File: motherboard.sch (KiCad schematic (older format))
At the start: 105 parts, among them P1 CONN_02X08, U1 STM32F411-LQFP64, U10 74LS125, U11 74LS125, U12 74LS125, U13 74LS125, U14 PCA9517A, U15 PCA9517A, U16 74LS125, U17 74LS125, U2 STM32F411-LQFP64, U3 AP7313, U4 74LS00, U5 74LS125, U6 FM25V20A-G, U7 FM25V20A-G, U8 FM25V20A-G, U9 FM25V20A-G, Y1 32k, Y2 8M(16pF), Y3 32k, Y4 8M(16pF)

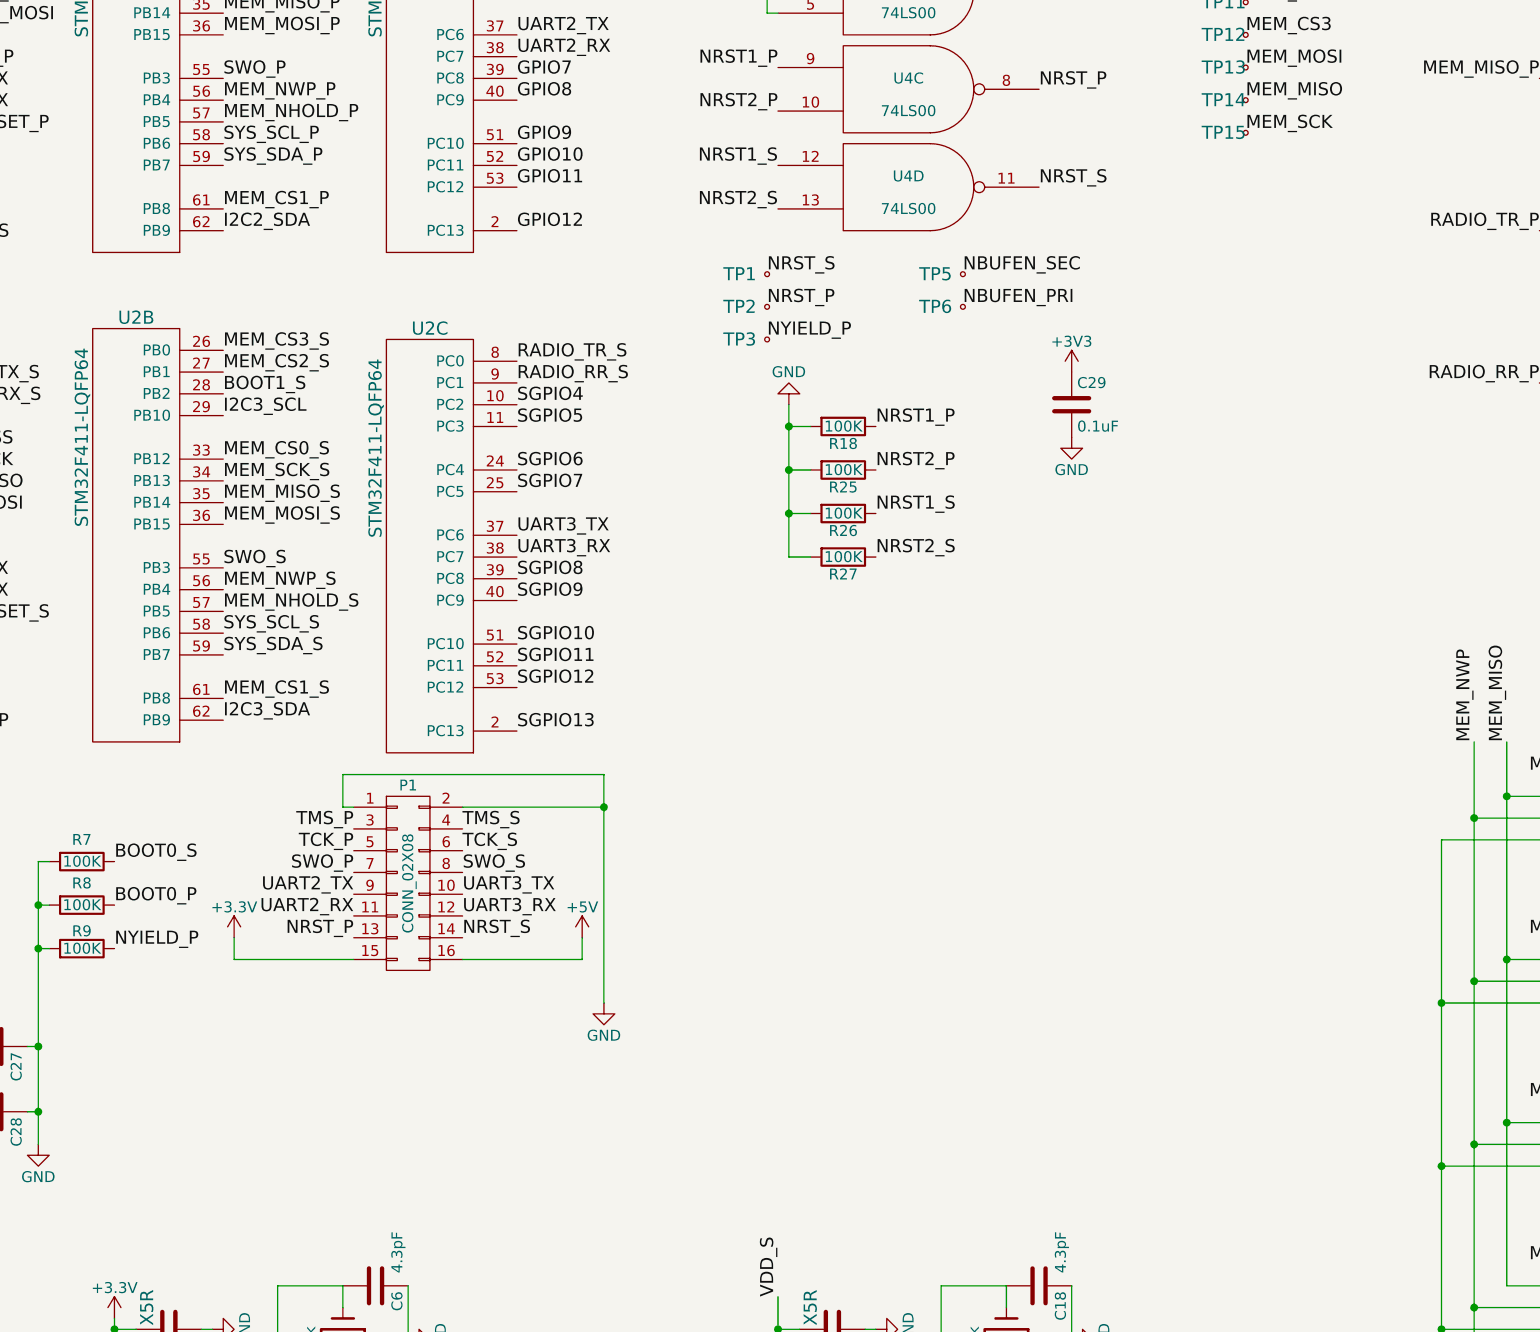
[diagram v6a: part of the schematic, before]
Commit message: Adding ground plane
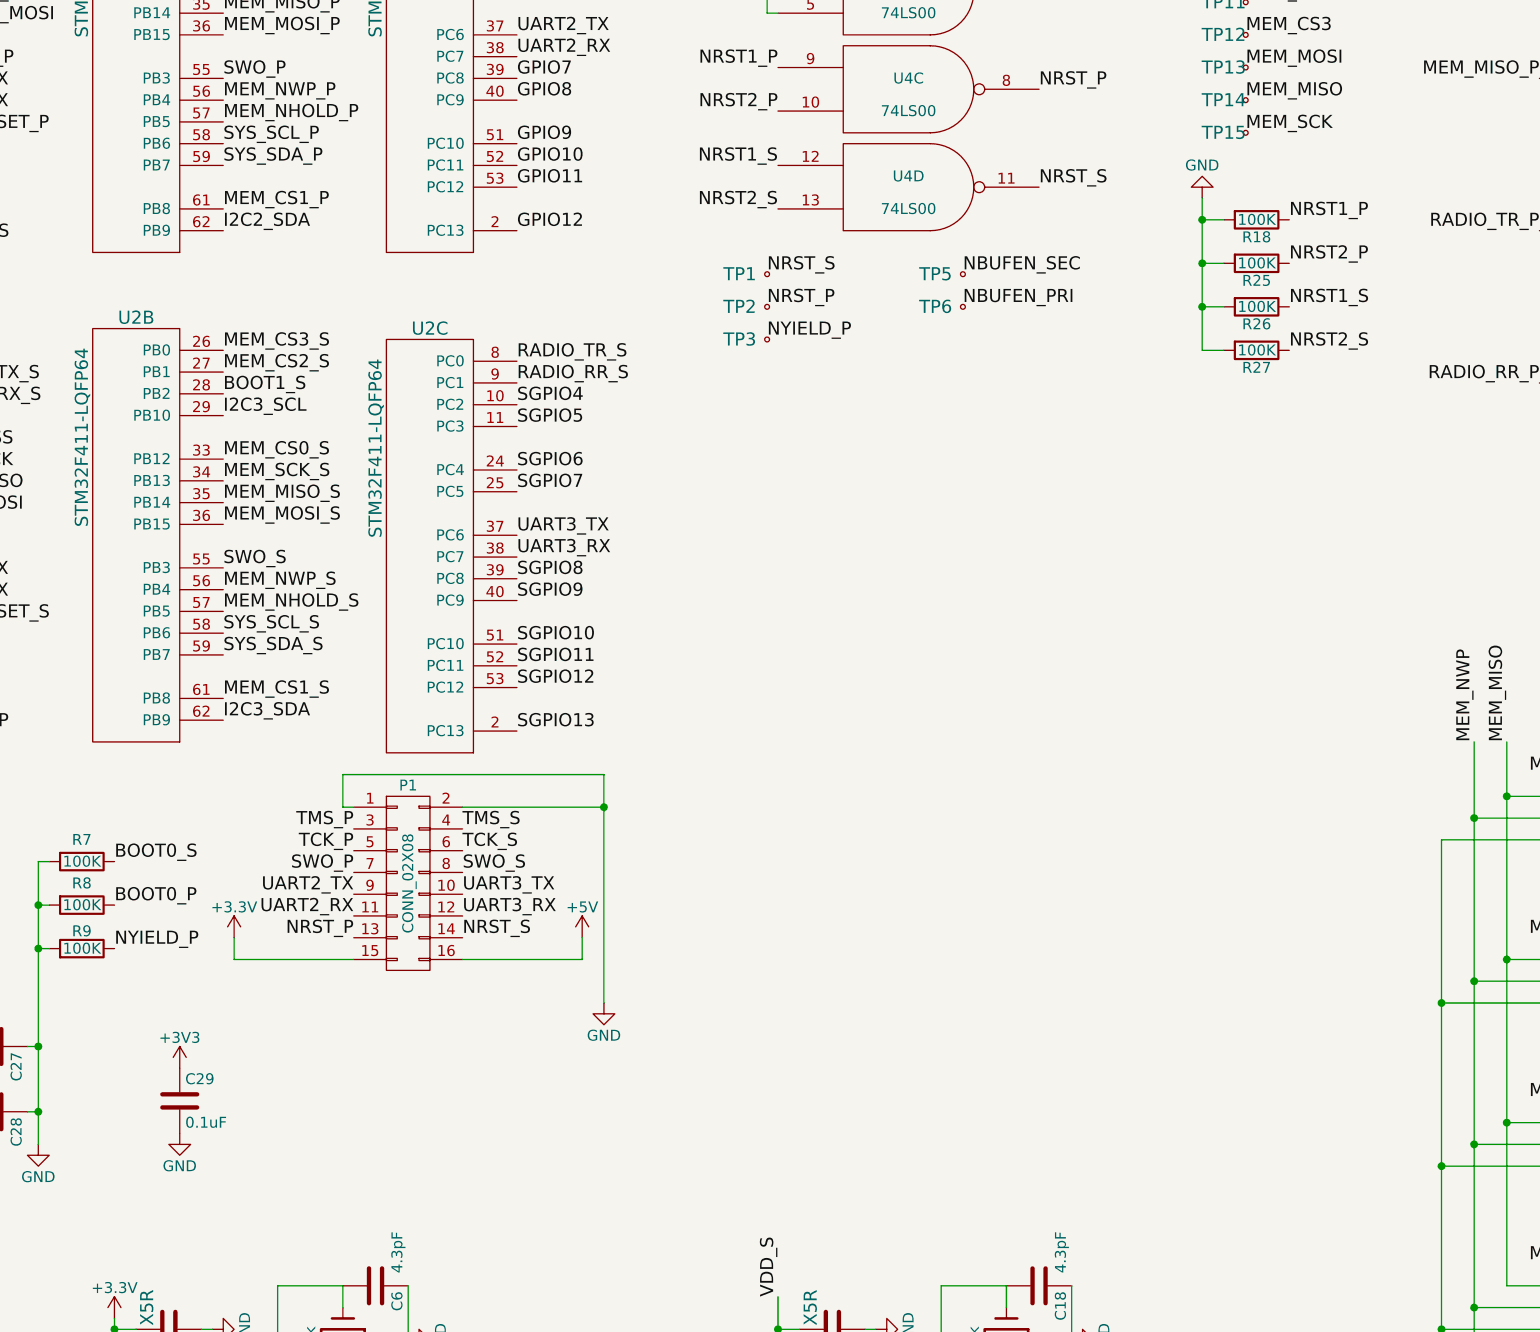
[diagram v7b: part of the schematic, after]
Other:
- moved on the sheet: C29, R18, R25, R26, R27
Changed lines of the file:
@@
 L R R18
 U 1 1 58FDD0DA
-P 5650 3400
-F 0 "R18" V 5730 3400 50  0000 C CNN
-F 1 "100K" V 5650 3400 50  0000 C CNN
-F 2 "Resistors_SMD:R_0805_HandSoldering" V 5580 3400 50  0001 C CNN
-F 3 "" H 5650 3400 50  0000 C CNN
-	1    5650 3400
+P 7550 2450
+F 0 "R18" V 7630 2450 50  0000 C CNN
+F 1 "100K" V 7550 2450 50  0000 C CNN
+F 2 "Resistors_SMD:R_0805_HandSoldering" V 7480 2450 50  0001 C CNN
+F 3 "" H 7550 2450 50  0000 C CNN
+	1    7550 2450
 	0    1    1    0
 $EndComp
@@
 L R R25
 U 1 1 58FF6AE5
-P 5650 3600
-F 0 "R25" V 5730 3600 50  0000 C CNN
-F 1 "100K" V 5650 3600 50  0000 C CNN
-F 2 "Resistors_SMD:R_0805_HandSoldering" V 5580 3600 50  0001 C CNN
-F 3 "" H 5650 3600 50  0000 C CNN
-	1    5650 3600
+P 7550 2650
+F 0 "R25" V 7630 2650 50  0000 C CNN
+F 1 "100K" V 7550 2650 50  0000 C CNN
+F 2 "Resistors_SMD:R_0805_HandSoldering" V 7480 2650 50  0001 C CNN
+F 3 "" H 7550 2650 50  0000 C CNN
+	1    7550 2650
 	0    1    1    0
 $EndComp
@@
 L R R26
 U 1 1 58FF6C71
-P 5650 3800
-F 0 "R26" V 5730 3800 50  0000 C CNN
-F 1 "100K" V 5650 3800 50  0000 C CNN
-F 2 "Resistors_SMD:R_0805_HandSoldering" V 5580 3800 50  0001 C CNN
-F 3 "" H 5650 3800 50  0000 C CNN
-	1    5650 3800
+P 7550 2850
+F 0 "R26" V 7630 2850 50  0000 C CNN
+F 1 "100K" V 7550 2850 50  0000 C CNN
+F 2 "Resistors_SMD:R_0805_HandSoldering" V 7480 2850 50  0001 C CNN
+F 3 "" H 7550 2850 50  0000 C CNN
+	1    7550 2850
 	0    1    1    0
 $EndComp
@@
 L R R27
 U 1 1 58FF6DFC
-P 5650 4000
-F 0 "R27" V 5730 4000 50  0000 C CNN
-F 1 "100K" V 5650 4000 50  0000 C CNN
-F 2 "Resistors_SMD:R_0805_HandSoldering" V 5580 4000 50  0001 C CNN
-F 3 "" H 5650 4000 50  0000 C CNN
-	1    5650 4000
-	0    1    1    0
-$EndComp
-Wire Wire Line
-	5500 3400 5400 3400
-Wire Wire Line
-	5400 4000 5500 4000
-Wire Wire Line
-	5500 3800 5400 3800
-Connection ~ 5400 3800
-Wire Wire Line
-	5500 3600 5400 3600
-Connection ~ 5400 3600
-Text Label 5800 3400 0    60   ~ 0
+P 7550 3050
+F 0 "R27" V 7630 3050 50  0000 C CNN
+F 1 "100K" V 7550 3050 50  0000 C CNN
+F 2 "Resistors_SMD:R_0805_HandSoldering" V 7480 3050 50  0001 C CNN
+F 3 "" H 7550 3050 50  0000 C CNN
+	1    7550 3050
+	0    1    1    0
+$EndComp
+Wire Wire Line
+	7400 2450 7300 2450
+Wire Wire Line
+	7300 3050 7400 3050
+Wire Wire Line
+	7400 2850 7300 2850
+Connection ~ 7300 2850
+Wire Wire Line
+	7400 2650 7300 2650
+Connection ~ 7300 2650
+Text Label 7700 2450 0    60   ~ 0
 NRST1_P
-Text Label 5800 3600 0    60   ~ 0
+Text Label 7700 2650 0    60   ~ 0
 NRST2_P
-Text Label 5800 3800 0    60   ~ 0
+Text Label 7700 2850 0    60   ~ 0
 NRST1_S
-Text Label 5800 4000 0    60   ~ 0
+Text Label 7700 3050 0    60   ~ 0
 NRST2_S
 Wire Wire Line
-	5400 3300 5400 4000
-Connection ~ 5400 3400
+	7300 2350 7300 3050
+Connection ~ 7300 2450
 Wire Wire Line
 	14950 7000 15400 7000
@@
 L C C29
 U 1 1 5904FA74
-P 6700 3300
-F 0 "C29" H 6725 3400 50  0000 L CNN
-F 1 "0.1uF" H 6725 3200 50  0000 L CNN
-F 2 "Capacitors_SMD:C_0805_HandSoldering" H 6738 3150 50  0001 C CNN
-F 3 "" H 6700 3300 50  0000 C CNN
-	1    6700 3300
-	1    0    0    -1
-$EndComp
-$Comp
-L +3V3 #PWR057
+P 2600 6500
+F 0 "C29" H 2625 6600 50  0000 L CNN
+F 1 "0.1uF" H 2625 6400 50  0000 L CNN
+F 2 "Capacitors_SMD:C_0805_HandSoldering" H 2638 6350 50  0001 C CNN
+F 3 "" H 2600 6500 50  0000 C CNN
+	1    2600 6500
+	1    0    0    -1
+$EndComp
+$Comp
+L +3V3 #PWR056
 U 1 1 59050061
-P 6700 3150
-F 0 "#PWR057" H 6700 3000 50  0001 C CNN
-F 1 "+3V3" H 6700 3290 50  0000 C CNN
-F 2 "" H 6700 3150 50  0000 C CNN
-F 3 "" H 6700 3150 50  0000 C CNN
-	1    6700 3150
+P 2600 6350
+F 0 "#PWR056" H 2600 6200 50  0001 C CNN
+F 1 "+3V3" H 2600 6490 50  0000 C CNN
+F 2 "" H 2600 6350 50  0000 C CNN
+F 3 "" H 2600 6350 50  0000 C CNN
+	1    2600 6350
+	1    0    0    -1
+$EndComp
+$Comp
+L GND #PWR057
+U 1 1 5905037E
+P 2600 6650
+F 0 "#PWR057" H 2600 6400 50  0001 C CNN
+F 1 "GND" H 2600 6500 50  0000 C CNN
+F 2 "" H 2600 6650 50  0000 C CNN
+F 3 "" H 2600 6650 50  0000 C CNN
+	1    2600 6650
 	1    0    0    -1
 $EndComp
 $Comp
 L GND #PWR058
-U 1 1 5905037E
-P 6700 3450
-F 0 "#PWR058" H 6700 3200 50  0001 C CNN
-F 1 "GND" H 6700 3300 50  0000 C CNN
-F 2 "" H 6700 3450 50  0000 C CNN
-F 3 "" H 6700 3450 50  0000 C CNN
-	1    6700 3450
-	1    0    0    -1
-$EndComp
-$Comp
-L GND #PWR059
 U 1 1 5905285C
 P 15800 1850
-F 0 "#PWR059" H 15800 1600 50  0001 C CNN
+F 0 "#PWR058" H 15800 1600 50  0001 C CNN
 F 1 "GND" H 15800 1700 50  0000 C CNN
 F 2 "" H 15800 1850 50  0000 C CNN
@@
 Connection ~ 15400 1300
 $Comp
-L GND #PWR060
+L GND #PWR059
 U 1 1 590581E4
 P 11750 1850
-F 0 "#PWR060" H 11750 1600 50  0001 C CNN
+F 0 "#PWR059" H 11750 1600 50  0001 C CNN
 F 1 "GND" H 11750 1700 50  0000 C CNN
 F 2 "" H 11750 1850 50  0000 C CNN
@@
 Connection ~ 12050 1300
 $Comp
-L GND #PWR061
+L GND #PWR060
 U 1 1 5905B968
 P 15050 9550
-F 0 "#PWR061" H 15050 9300 50  0001 C CNN
+F 0 "#PWR060" H 15050 9300 50  0001 C CNN
 F 1 "GND" H 15050 9400 50  0000 C CNN
 F 2 "" H 15050 9550 50  0000 C CNN
@@
 Not Populated - Tie Down if Unused
 $Comp
-L GND #PWR062
+L GND #PWR061
 U 1 1 5900142E
 P 11750 2950
-F 0 "#PWR062" H 11750 2700 50  0001 C CNN
+F 0 "#PWR061" H 11750 2700 50  0001 C CNN
 F 1 "GND" H 11750 2800 50  0000 C CNN
 F 2 "" H 11750 2950 50  0000 C CNN
@@
 	11750 2400 11750 2500
 $Comp
-L GND #PWR063
+L GND #PWR062
 U 1 1 5900389F
 P 15800 2950
-F 0 "#PWR063" H 15800 2700 50  0001 C CNN
+F 0 "#PWR062" H 15800 2700 50  0001 C CNN
 F 1 "GND" H 15800 2800 50  0000 C CNN
 F 2 "" H 15800 2950 50  0000 C CNN
@@
 NoConn ~ 8900 10850
 $Comp
-L GND #PWR?
+L GND #PWR063
 U 1 1 5AC8ED6B
-P 5400 3300
-F 0 "#PWR?" H 5400 3050 50  0001 C CNN
-F 1 "GND" H 5400 3150 50  0000 C CNN
-F 2 "" H 5400 3300 50  0000 C CNN
-F 3 "" H 5400 3300 50  0000 C CNN
-	1    5400 3300
+P 7300 2350
+F 0 "#PWR063" H 7300 2100 50  0001 C CNN
+F 1 "GND" H 7300 2200 50  0000 C CNN
+F 2 "" H 7300 2350 50  0000 C CNN
+F 3 "" H 7300 2350 50  0000 C CNN
+	1    7300 2350
 	-1   0    0    1
 $EndComp

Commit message: Fixed pull-ups on NRST lines
Also fixed naming of RSTn_m lines.
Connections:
- net +3V3: no longer R1.2, R2.2, R3.2, R4.2, R5.2, R6.2
- net GND: now also C33.2, C35.2
- net NBUFEN_SEC: now also C33.1, C35.1
- net NRST_P: now also R3.2; no longer R3.1, U4.8
- net NRST_S: now also R4.2; no longer R4.1, U4.11
- net SGPIO0: no longer H2.1 (P1)
- net SGPIO1: no longer H2.2 (P2)
- net SGPIO10: no longer H1.36 (P36)
- net SGPIO11: no longer H1.37 (P37)
- net SGPIO12: no longer H1.38 (P38)
- net SGPIO13: no longer H1.39 (P39)
- net SGPIO2: no longer H2.3 (P3)
- net SGPIO3: no longer H2.4 (P4)
- net SGPIO4: no longer H2.7 (P7)
- net SGPIO5: no longer H1.50 (P50)
- net SGPIO6: no longer H1.52 (P52)
- net SGPIO7: no longer H1.33 (P33)
- net SGPIO8: no longer H1.34 (P34)
- net SGPIO9: no longer H1.35 (P35)
- net NRST1_P renamed RST1_P
- net NRST1_S renamed RST1_S
- net NRST2_P renamed RST2_P
- net NRST2_S renamed RST2_S
- new net: R3.1, U4.8
- new net: R1.2, R2.2, R5.2, R6.2
- new net: R4.1, U4.11
- no-connect marks 42 -> 70
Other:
- moved on the sheet: R18, R19, R20, R21, R22, R23, R24, R25, R26, R27, R3, R4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
